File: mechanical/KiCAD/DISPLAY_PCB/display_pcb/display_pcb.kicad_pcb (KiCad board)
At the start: 2 copper layers, 50 x 50 mm, 54 parts, among them J1 USB_C_Receptacle_USB2.0_16P, J2 Conn_01x18_Socket, J3 Conn_01x01_Pin, J4 Conn_01x01_Pin, J5 Conn_01x02_Pin, Q1 AO3401A, Q2 FS8205, U1 ESP32-S3-WROOM-1, U2 DW01A, U3 USBLC6-2P6, U4 TP4056-42-ESOP8, U5 TLV75733PDBV

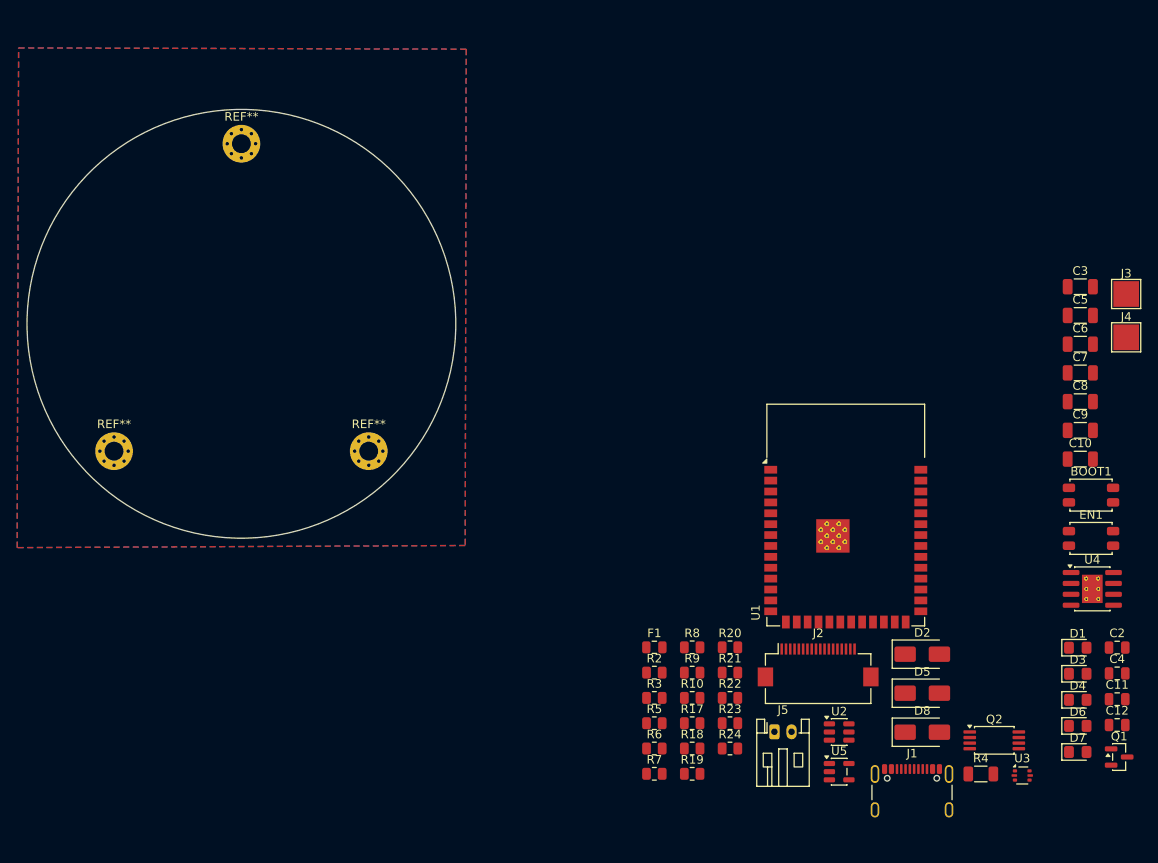
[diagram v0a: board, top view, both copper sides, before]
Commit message: Related components are grouped together, they are roughly placed on the PCB. The battery protection may have to go due space limitations (most LiPO batteries has built-in protection). The PCB will be spaced out with extra spacers so the current keepout zones on the front copper face may be used.
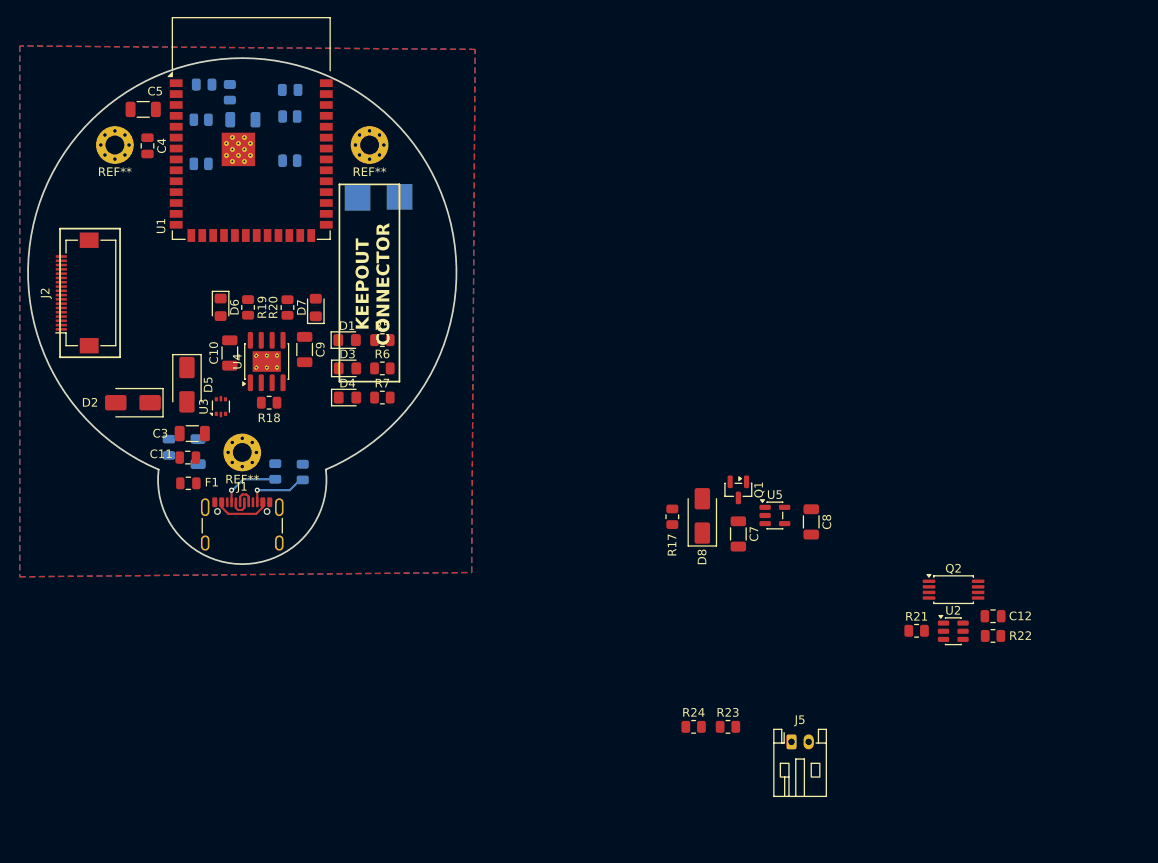
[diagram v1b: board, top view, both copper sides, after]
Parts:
- BOOT1, C2, C6, EN1, J3, J4, R10, R2, R3, R4, R8, R9: moved to B.Cu
- moved C4 128.7 mm to (73.9, 36.0), turned to -90 degrees
- moved EN1 113.6 mm to (80.2, 35.6), turned to -90 degrees
- moved C2 113.0 mm to (76.4, 71.2), turned to 90 degrees
- moved C11 112.0 mm to (78.6, 72.4), turned to 180 degrees
- moved C5 111.9 mm to (73.4, 31.8), turned to 180 degrees
- moved D6 111.2 mm to (82.4, 54.9), turned to -90 degrees
- moved C3 105.0 mm to (79.1, 69.6), turned to 180 degrees
- moved U3 102.9 mm to (82.5, 66.5), turned to 90 degrees
- moved D7 102.9 mm to (93.5, 54.9), turned to 90 degrees
- moved BOOT1 102.3 mm to (90.5, 35.2), turned to 90 degrees
- moved C6 101.1 mm to (85.0, 33.0), turned to 180 degrees
- moved C10 99.9 mm to (83.5, 60.2), turned to 90 degrees
- moved U4 99.9 mm to (87.8, 61.2), turned to 90 degrees
- moved R4 98.7 mm to (79.8, 71.7), turned to 90 degrees
- moved J2 96.7 mm to (65.7, 53.2), turned to 90 degrees
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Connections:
- BOOT1 pad 1: Net-(BOOT1-Pad1) -> BOOT
- BOOT1 pad 2: Net-(BOOT1-Pad1) -> GND
- EN1 pad 2: Net-(EN1-Pad1) -> GND
- R8 pad 2: Net-(EN1-A) -> Net-(EN1-Pad1)
- R9 pad 1: Net-(EN1-A) -> Net-(EN1-Pad1)
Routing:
- net Net-(J1-CC2): track 0.00 -> 6.91 mm, vias 0 -> 1
- net Net-(J1-CC1): track 0.00 -> 6.74 mm, vias 0 -> 1
- net Net-(F1-Pad1): track 0.00 -> 6.59 mm
- net Net-(J1-D--PadA7): track 0.00 -> 2.50 mm
- net Net-(J1-D+-PadA6): track 0.00 -> 2.50 mm
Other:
- board size 50 x 50 mm -> 50 x 59 mm
- board text added: "KEEPOUT"
- board text added: "KEEPOUT CONNECTOR"
- board text added: "PLACE FOR BATTERY"

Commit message: The components are placed, the flex cable connector pinout has to be changed, the protection circuit was deleted because of limited space.
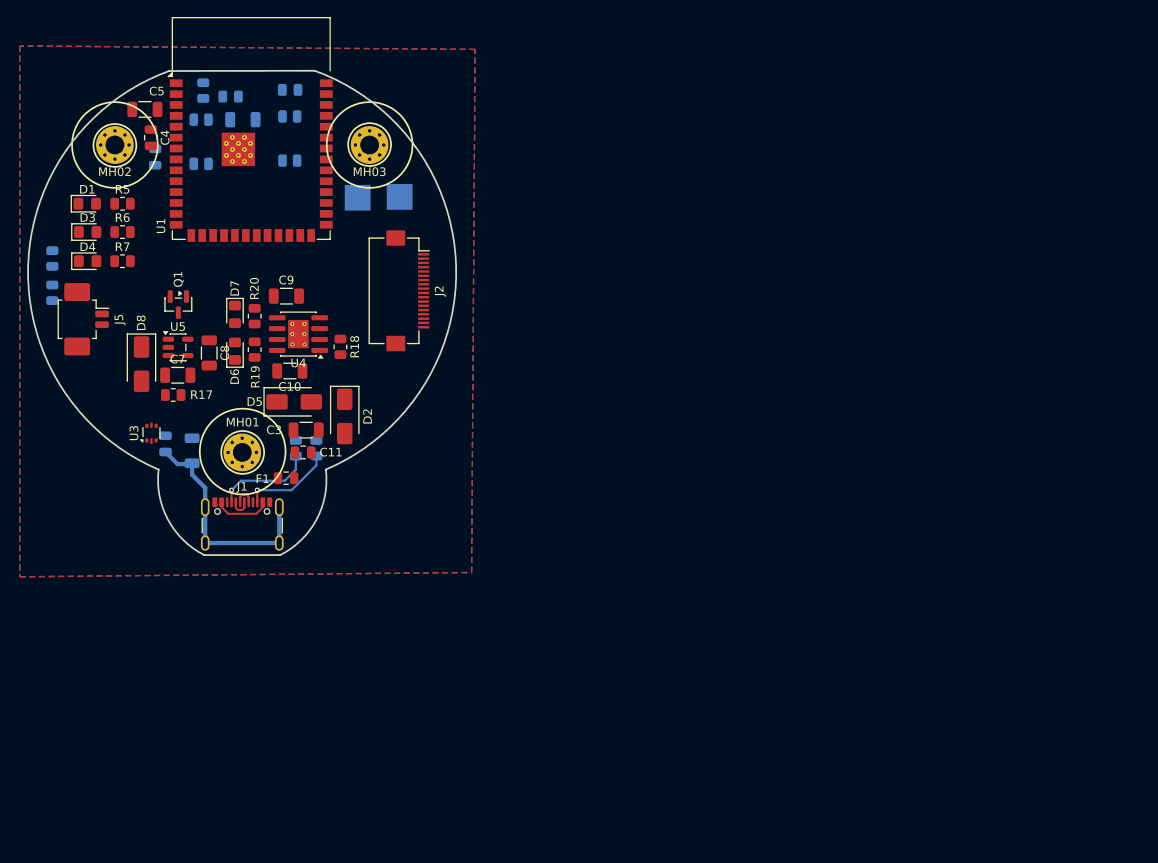
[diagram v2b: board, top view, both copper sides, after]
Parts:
- removed C12: 100nF, Capacitor_SMD:C_0805_2012Metric
- removed Q2: FS8205, Package_SO:TSSOP-8_4.4x3mm_P0.65mm
- removed R21: 2K, Resistor_SMD:R_0805_2012Metric
- removed R22: 470R, Resistor_SMD:R_0805_2012Metric
- removed U2: DW01A, Package_TO_SOT_SMD:SOT-23-6
- added C13: 10nF, Capacitor_SMD:C_0805_2012Metric, B.Cu at (74.8, 37.4)
- D7: value LED_R -> LED_G
- J5: footprint Connector_JST:JST_PH_S2B-PH-K_1x02_P2.00mm_Horizontal -> Connector_Molex:Molex_PicoBlade_53261-0271_1x02-1MP_P1.25mm_Horizontal
- R23, R24: moved to B.Cu
- moved J5 96.4 mm to (66.2, 56.3), turned to -90 degrees
- moved R23 93.6 mm to (62.8, 53.2), turned to -90 degrees
- moved R24 92.6 mm to (62.8, 49.2), turned to -90 degrees
- moved C8 72.9 mm to (81.1, 60.2)
- moved U5 72.3 mm to (77.5, 59.5)
- moved Q1 68.8 mm to (77.5, 54.6)
- moved C7 67.9 mm to (77.4, 62.8), turned to 0 degrees
- moved D8 67.8 mm to (73.2, 61.5), turned to -90 degrees
- moved R17 59.9 mm to (76.9, 65.1), turned to 0 degrees
- moved J2 38.6 mm to (104.2, 53.0), turned to -90 degrees
- moved D1 34.2 mm to (66.9, 42.8)
- moved D3 34.2 mm to (66.9, 46.1)
- moved D4 34.2 mm to (66.9, 49.5)
- moved R5 34.2 mm to (71.0, 42.8)
- moved R6 34.2 mm to (71.0, 46.1)
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- renumbered REF** to MH01, REF** to MH02, REF** to MH03
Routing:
- net Net-(J1-SHIELD): track 0.00 -> 26.5 mm
- net Net-(J1-CC1): track 6.74 -> 11.6 mm
- net Net-(J1-CC2): track 6.91 -> 10.6 mm
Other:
- board size 50 x 59 mm -> 49.9 x 56.5 mm
- board text removed: "KEEPOUT CONNECTOR"

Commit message: Main power lines are connected, the USB ESD protection IC and the flex cable connector is not yet wired. Some components may need some more layout fixing.
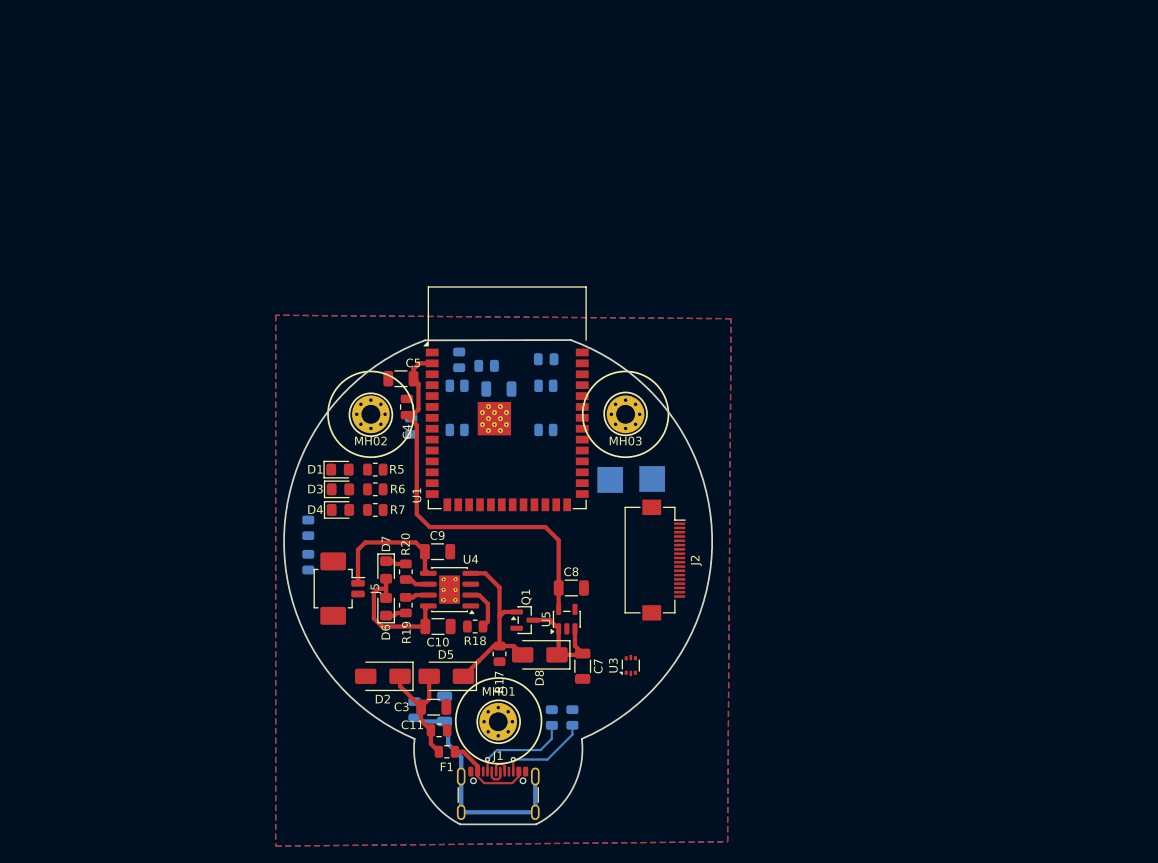
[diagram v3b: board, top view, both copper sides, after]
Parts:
- moved U3 62.1 mm to (130.3, 96.7)
- moved C7 58.1 mm to (124.7, 96.7), turned to -90 degrees
- moved D8 57.5 mm to (119.7, 95.4), turned to 180 degrees
- moved U5 55.3 mm to (122.8, 91.2), turned to 90 degrees
- moved Q1 54.6 mm to (117.9, 91.4), turned to 0 degrees
- moved C8 50.3 mm to (123.3, 87.6), turned to 0 degrees
- moved R17 48.6 mm to (115.0, 95.3), turned to -90 degrees
- moved J4 44.2 mm to (127.9, 75.0)
- moved J3 44.2 mm to (132.8, 74.9)
- moved BOOT1 43.3 mm to (120.4, 66.6)
- moved C13 43.3 mm to (104.7, 68.8)
- moved C4 43.3 mm to (104.2, 66.5), turned to 90 degrees
- moved C5 43.3 mm to (103.5, 63.2)
- moved MH02 43.3 mm to (100.0, 67.4)
- moved MH03 43.3 mm to (129.7, 67.4)
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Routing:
- net +3.3V: track 0.00 -> 46.9 mm
- net +5V: track 0.00 -> 37.7 mm
- net BTR +: track 0.00 -> 15.2 mm
- net Net-(D2-A1): track 0.00 -> 14.7 mm
- net Net-(D8-K): track 0.00 -> 12.9 mm
- net Net-(U4-PROG): track 0.00 -> 5.30 mm
- net Net-(F1-Pad1): track 6.59 -> 10.6 mm
- net Net-(U4-~{STDBY}): track 0.00 -> 2.85 mm
- net Net-(U4-~{CHRG}): track 0.00 -> 2.73 mm
- net Net-(D7-K): track 0.00 -> 2.43 mm
- net Net-(D6-K): track 0.00 -> 2.42 mm
- net Net-(J1-SHIELD): track 26.5 -> 27.9 mm
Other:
- board text added: "40.5 x 30 mm"

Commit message: Relocated some components for the high signal routes, the flex cable connector is still not in a fixed location. The buttons and the LEDs may have to be relocated for easier routing.
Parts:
- R18: value 3K -> 2.4K
- moved J3 20.0 mm to (112.8, 73.8)
- moved U3 10.5 mm to (122.0, 103.0)
- moved J4 10.3 mm to (117.6, 73.8)
- moved J5 3.39 mm to (94.8, 84.5)
- moved C8 3.00 mm to (120.3, 87.6), turned to 180 degrees
- moved C13 2.08 mm to (105.2, 66.8), turned to 90 degrees
- moved C10 1.96 mm to (107.0, 93.9)
- moved R18 1.96 mm to (111.3, 93.9)
- moved R19 1.96 mm to (103.2, 91.4)
- moved U4 1.96 mm to (108.3, 89.6)
- moved C9 1.96 mm to (106.9, 85.2)
- moved D6 1.96 mm to (100.9, 91.6)
- moved D7 1.96 mm to (100.9, 87.3)
- moved R20 1.96 mm to (103.2, 87.5)
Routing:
- net USB_D-: track 0.00 -> 48.1 mm
- net USB_D+: track 0.00 -> 47.6 mm
- net BTR +: track 15.2 -> 42.9 mm, vias 0 -> 2
- net BTR CHRG: track 0.00 -> 25.5 mm, vias 0 -> 1
- net Net-(D2-A1): track 14.7 -> 32.4 mm
- net Net-(J3-Pin_1): track 0.00 -> 16.4 mm, vias 0 -> 1
- net Net-(J4-Pin_1): track 0.00 -> 16.1 mm, vias 0 -> 1
- net +3.3V: track 46.9 -> 59.8 mm, vias 0 -> 1
- net BOOT: track 0.00 -> 12.0 mm, vias 0 -> 1
- net Net-(J1-D--PadA7): track 2.50 -> 12.8 mm
- net GND: track 0.00 -> 10.2 mm, vias 0 -> 20
- net EN: track 0.00 -> 10.1 mm, vias 0 -> 1
- net Net-(EN1-Pad1): track 0.00 -> 10.1 mm
- net +5V: track 37.7 -> 47.5 mm
- net Net-(J1-D+-PadA6): track 2.50 -> 11.9 mm
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
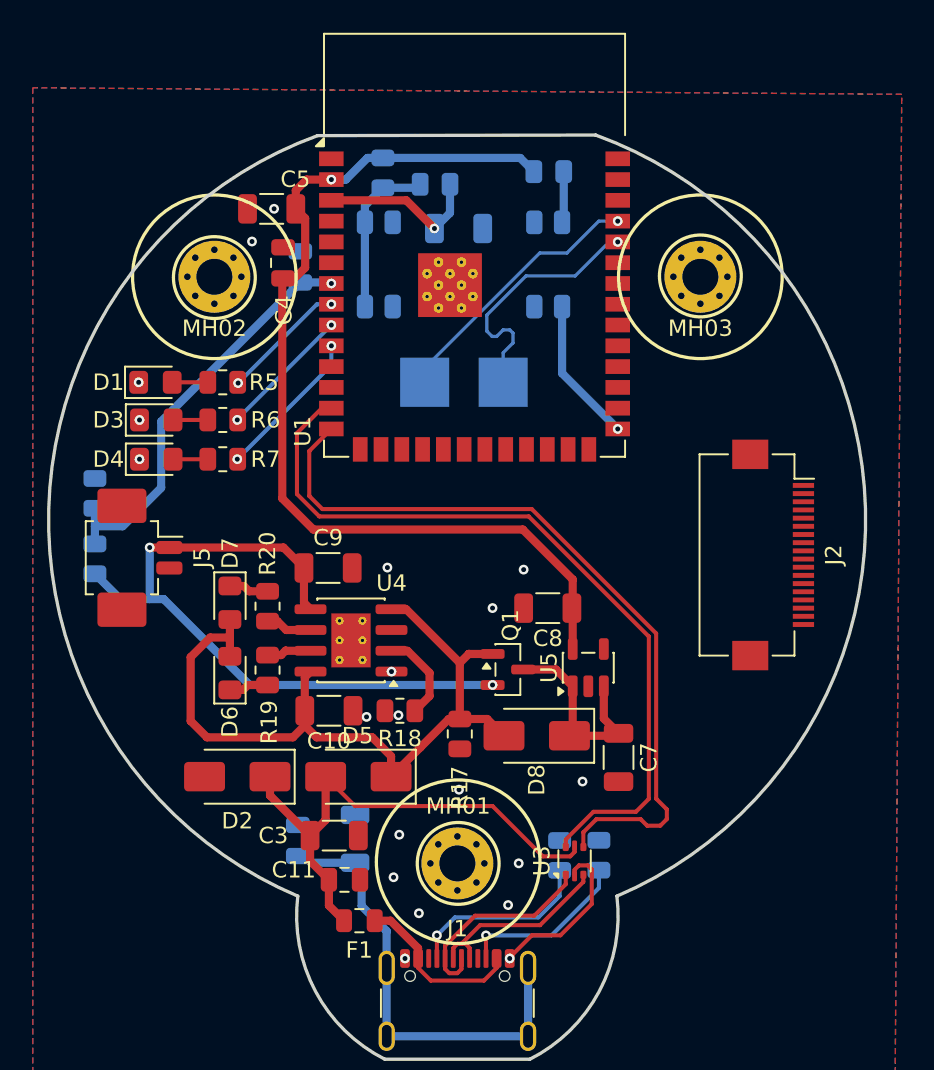
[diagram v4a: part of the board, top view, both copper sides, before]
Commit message: Display PCB is basically finished, all routes are connected, all data lines should be within the length difference tolerance level, some spacing tolerances are still not fixed.
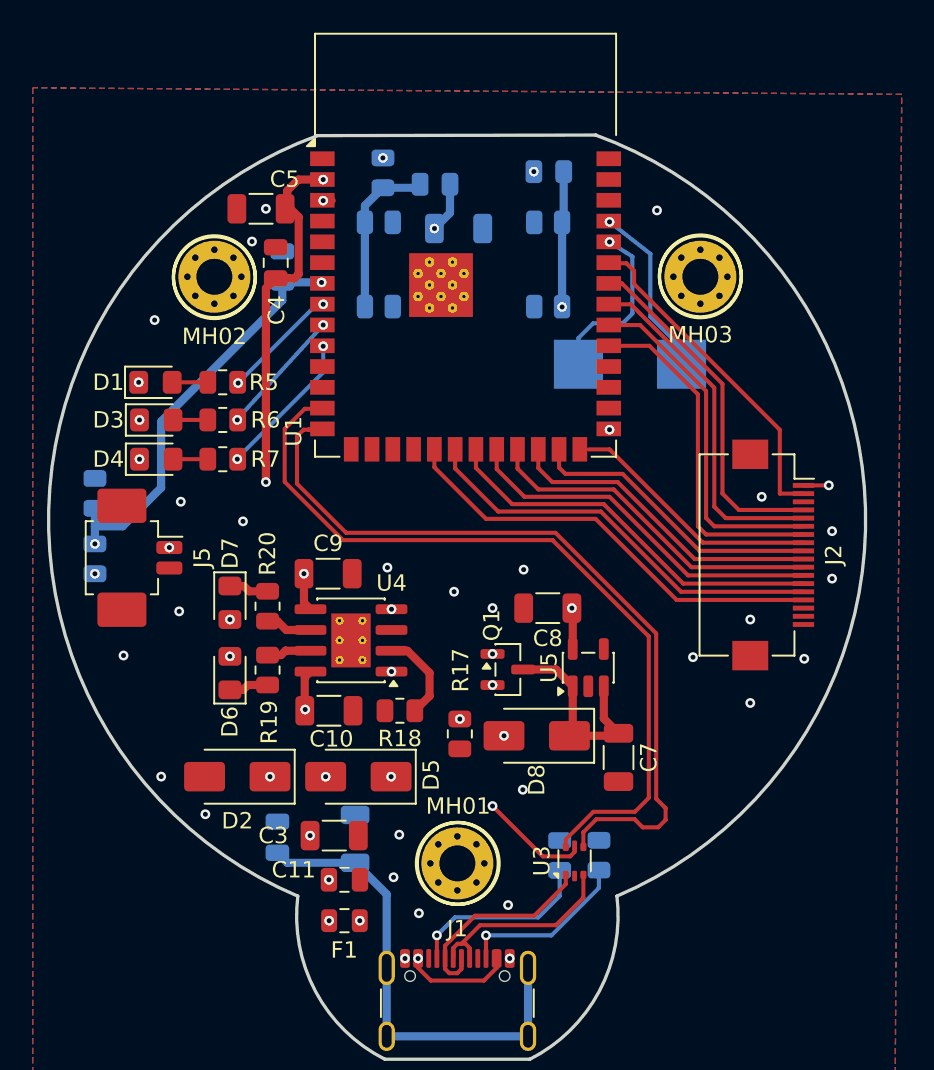
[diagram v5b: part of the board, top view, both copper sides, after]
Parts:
- moved J3 15.7 mm to (128.5, 72.7)
- moved J4 4.73 mm to (122.2, 72.7)
- moved C2 1.27 mm to (103.8, 101.6)
- moved C13 1.10 mm to (104.1, 66.8)
- moved F1 0.91 mm to (107.9, 106.7)
- moved C5 0.65 mm to (102.8, 63.2)
- moved U1 0.55 mm to (115.3, 65.4)
- moved C4 0.45 mm to (103.7, 66.5)
- moved C9 0.35 mm to (106.9, 85.5)
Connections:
- U1 pad 12: LCD_TE -> unconnected-(U1-IO8-Pad12)
- U1 pad 15: TP_SDA -> unconnected-(U1-IO3-Pad15)
- U1 pad 17: LCD_IO3 -> unconnected-(U1-IO9-Pad17)
- U1 pad 18: LCD_CS -> unconnected-(U1-IO10-Pad18)
- U1 pad 19: LCD_IO0 -> TP_INT
- U1 pad 20: LCD_SCLK -> TP_SDA
- U1 pad 21: LCD_IO1 -> TP_SCL
- U1 pad 22: LCD_IO2 -> TP_RST
- U1 pad 23: LCD_RST -> LCD_IO3
- U1 pad 24: unconnected-(U1-IO47-Pad24) -> LCD_TE
- U1 pad 25: unconnected-(U1-IO48-Pad25) -> LCD_CS
- U1 pad 26: unconnected-(U1-IO45-Pad26) -> LCD_RST
- U1 pad 31: unconnected-(U1-IO38-Pad31) -> LCD_IO2
- U1 pad 32: unconnected-(U1-IO39-Pad32) -> LCD_IO1
- U1 pad 33: unconnected-(U1-IO40-Pad33) -> LCD_IO0
- U1 pad 34: unconnected-(U1-IO41-Pad34) -> LCD_SCLK
- U1 pad 35: unconnected-(U1-IO42-Pad35) -> LCD_BL
- U1 pad 38: TP_SCL -> unconnected-(U1-IO2-Pad38)
- U1 pad 4: LCD_BL -> unconnected-(U1-IO4-Pad4)
- U1 pad 5: TP_INT -> unconnected-(U1-IO5-Pad5)
- U1 pad 6: TP_RST -> unconnected-(U1-IO6-Pad6)
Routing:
- net TP_INT: track 0.00 -> 27.0 mm
- net TP_SDA: track 0.00 -> 25.5 mm
- net TP_SCL: track 0.00 -> 24.0 mm
- net TP_RST: track 0.00 -> 22.6 mm
- net +3.3V: track 59.8 -> 81.2 mm, vias 1 -> 6
- net LCD_IO3: track 0.00 -> 21.1 mm
- net LCD_IO0: track 0.00 -> 21.0 mm
- net LCD_SCLK: track 0.00 -> 21.0 mm
- net LCD_IO1: track 0.00 -> 21.0 mm
- net LCD_IO2: track 0.00 -> 20.8 mm
- net LCD_BL: track 0.00 -> 20.5 mm
- net LCD_TE: track 0.00 -> 19.6 mm
- net LCD_CS: track 0.00 -> 18.1 mm
- net LCD_RST: track 0.00 -> 15.5 mm
- net GND: track 10.2 -> 0.00 mm, vias 20 -> 32
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- added copper zone on In1.Cu, net GND
- added copper zone on In2.Cu, net GND
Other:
- copper layers 2 -> 4

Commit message: OBD and displa PCB are both basically finished, some files has to be generated and the PCBs can be ordered. Documentation should be the next step.
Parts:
- moved C13 7.21 mm to (98.5, 71.3), turned to 180 degrees
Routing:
- net LCD_RST: track 15.5 -> 16.0 mm
- net BTR CHRG: track 25.6 -> 26.1 mm, vias 2 -> 1
- net +3.3V: track 81.2 -> 81.1 mm, vias 6 -> 7
- net GND: vias 32 -> 47
